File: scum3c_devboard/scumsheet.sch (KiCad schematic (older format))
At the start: 18 parts, among them P5 Conn_01x02, U7 ADT7302ARMZ, U8 scum3

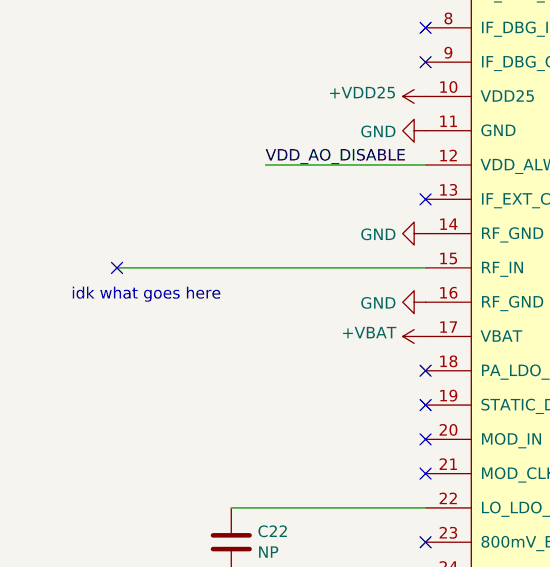
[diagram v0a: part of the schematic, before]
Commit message: added SMA
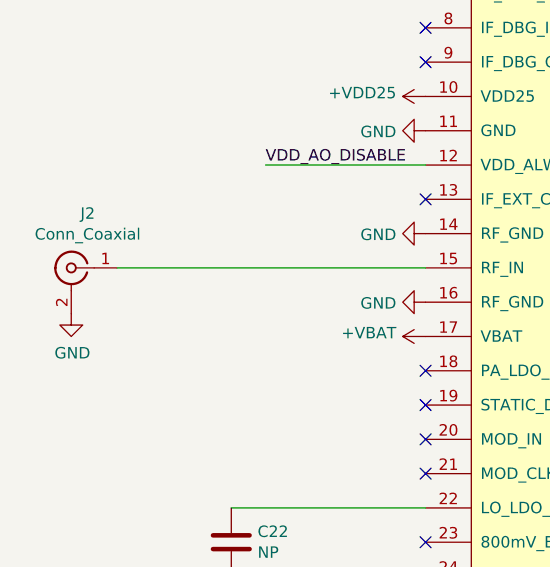
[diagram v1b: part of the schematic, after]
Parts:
- added J2: Conn_Coaxial, Connector_Coaxial:SMA_Amphenol_132134-14_Vertical, symbol Connector:Conn_Coaxial
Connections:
- net GND: now also J2.2 (Ext)
- net at U8.15 (RF_IN): now also J2.1 (In)
- no-connect marks 47 -> 46
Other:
- note removed: "idk what goes here"
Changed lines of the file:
@@
 Wire Wire Line
 	2250 4100 900  4100
-Text Notes 700  4250 0    50   ~ 0
-idk what goes here
 $Comp
 L Device:R_US R13
@@
 Text Label 4750 6350 1    50   ~ 0
 GP7
-NoConn ~ 900  4100
+$Comp
+L Connector:Conn_Coaxial J2
+U 1 1 5F3FC09A
+P 700 4100
+F 0 "J2" H 628 4338 50  0000 C CNN
+F 1 "Conn_Coaxial" H 628 4247 50  0000 C CNN
+F 2 "Connector_Coaxial:SMA_Amphenol_132134-14_Vertical" H 700 4100 50  0001 C CNN
+F 3 " ~" H 700 4100 50  0001 C CNN
+	1    700  4100
+	-1   0    0    -1
+$EndComp
+$Comp
+L power:GND #PWR0212
+U 1 1 5F3FE6A2
+P 700 4300
+F 0 "#PWR0212" H 700 4050 50  0001 C CNN
+F 1 "GND" H 705 4127 50  0000 C CNN
+F 2 "" H 700 4300 50  0001 C CNN
+F 3 "" H 700 4300 50  0001 C CNN
+	1    700  4300
+	1    0    0    -1
+$EndComp
 $EndSCHEMATC

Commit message: replaced placeholder scum footprint with 12x12 mm
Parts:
- U8: footprint SCUM:QFP-100_2x3_Pitch0.15mm -> SCUM:QFN-100_EP_12x12_Pitch0.4mm
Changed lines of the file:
@@
 F 0 "U8" H 8944 3271 50  0000 L CNN
 F 1 "scum3" H 8944 3180 50  0000 L CNN
-F 2 "SCUM:QFP-100_2x3_Pitch0.15mm" H 5200 3450 50  0001 C CNN
+F 2 "SCUM:QFN-100_EP_12x12_Pitch0.4mm" H 5200 3450 50  0001 C CNN
 F 3 "" H 5200 3450 50  0001 C CNN
 	1    5200 3450

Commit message: changed resistor smd footprint to 0402
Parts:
- R12, R13, R14: footprint Resistor_SMD:R_0603_1608Metric -> Resistor_SMD:R_0402_1005Metric
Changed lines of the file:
@@
 F 0 "R13" H 9968 1896 50  0000 L CNN
 F 1 "NP" H 9968 1805 50  0000 L CNN
-F 2 "Resistor_SMD:R_0603_1608Metric" V 9940 1840 50  0001 C CNN
+F 2 "Resistor_SMD:R_0402_1005Metric" V 9940 1840 50  0001 C CNN
 F 3 "~" H 9900 1850 50  0001 C CNN
 	1    9900 1850
@@
 F 0 "R14" H 10618 1896 50  0000 L CNN
 F 1 "NP" H 10618 1805 50  0000 L CNN
-F 2 "Resistor_SMD:R_0603_1608Metric" V 10590 1840 50  0001 C CNN
+F 2 "Resistor_SMD:R_0402_1005Metric" V 10590 1840 50  0001 C CNN
 F 3 "~" H 10550 1850 50  0001 C CNN
 	1    10550 1850
@@
 F 0 "R12" H 5718 746 50  0000 L CNN
 F 1 "NP" H 5718 655 50  0000 L CNN
-F 2 "Resistor_SMD:R_0603_1608Metric" V 5690 690 50  0001 C CNN
+F 2 "Resistor_SMD:R_0402_1005Metric" V 5690 690 50  0001 C CNN
 F 3 "~" H 5650 700 50  0001 C CNN
 	1    5650 700
